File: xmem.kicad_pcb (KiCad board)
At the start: 2 copper layers, 6 parts, among them P1 CONN_02X18, U1 AS6C1008-55SIN, U2 SN74AHC573

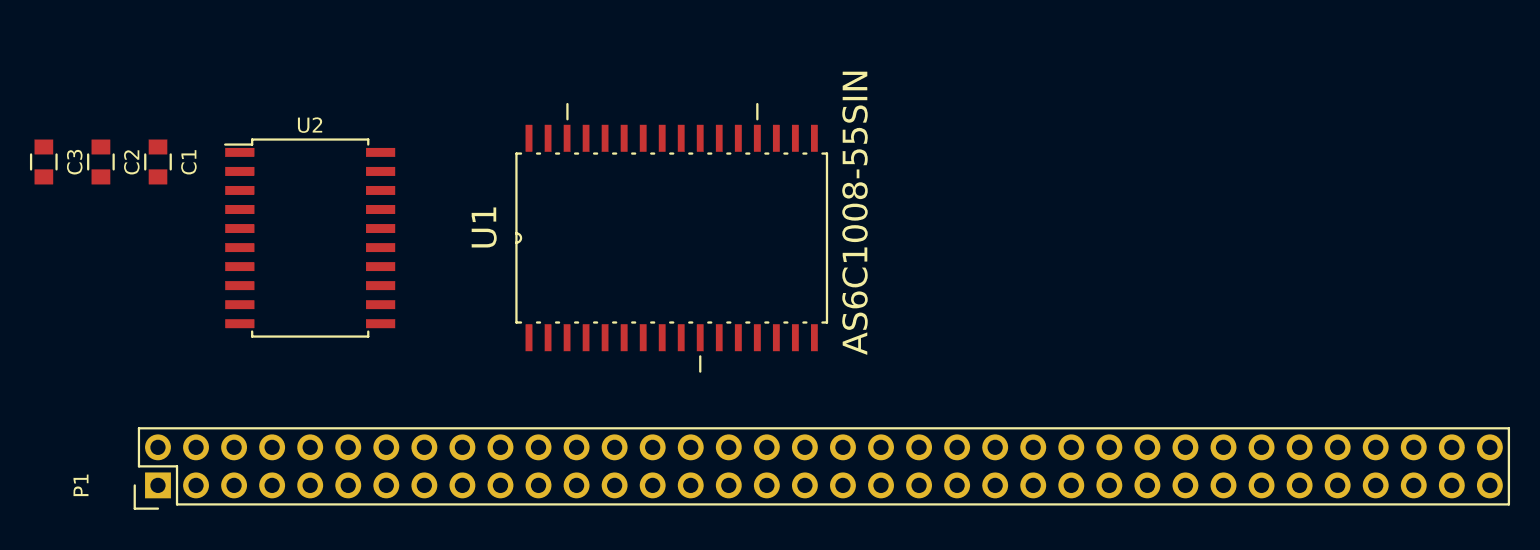
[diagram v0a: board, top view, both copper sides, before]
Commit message: Update to connect remaining pins and update footprints
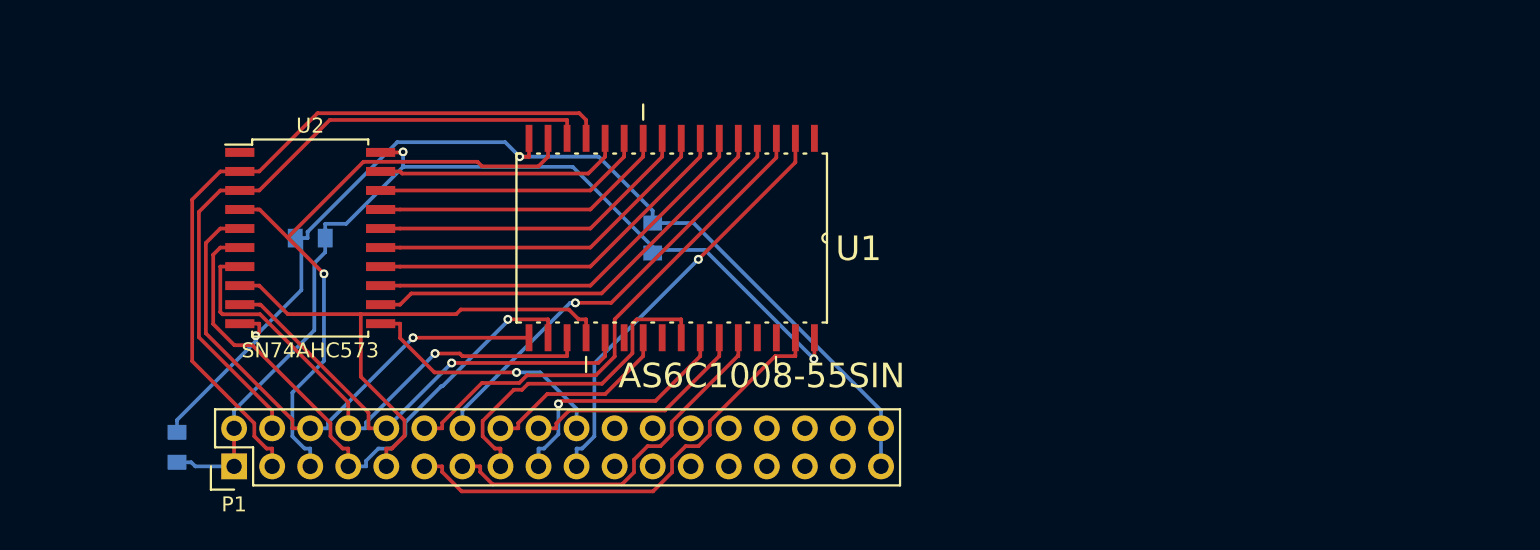
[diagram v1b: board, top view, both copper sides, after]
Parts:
- C1, C2, C3: moved to B.Cu
- P1: footprint Pin_Headers:Pin_Header_Straight_2x36 -> Pin_Headers:Pin_Header_Straight_2x18
- moved C2 37.2 mm to (139.7, 104.1), turned to 90 degrees
- moved C3 21.0 mm to (108.0, 118.1), turned to 90 degrees
- moved C1 11.4 mm to (116.8, 104.1), turned to 180 degrees
- moved P1 5.24 mm to (111.8, 119.4)
- turned U1 to 270 degrees
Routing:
- net GND: track 0.00 -> 74.1 mm, vias 0 -> 2
- net VCC: track 0.00 -> 66.4 mm, vias 0 -> 2
- net /D0: track 0.00 -> 50.3 mm
- net /D1: track 0.00 -> 44.8 mm
- net /D2: track 0.00 -> 42.9 mm, vias 0 -> 1
- net /D4: track 0.00 -> 40.2 mm, vias 0 -> 1
- net /D6: track 0.00 -> 37.6 mm
- net /D3: track 0.00 -> 35.9 mm, vias 0 -> 1
- net /D5: track 0.00 -> 35.3 mm, vias 0 -> 1
- net /A14: track 0.00 -> 33.9 mm
- net /A15: track 0.00 -> 31.7 mm
- net /D7: track 0.00 -> 31.6 mm, vias 0 -> 1
- net /A7: track 0.00 -> 29.2 mm
- net /A12: track 0.00 -> 29.1 mm, vias 0 -> 1
- net /A16: track 0.00 -> 28.2 mm, vias 0 -> 1
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
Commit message: Add flood fill ground plane. Fix close tracks. Add text
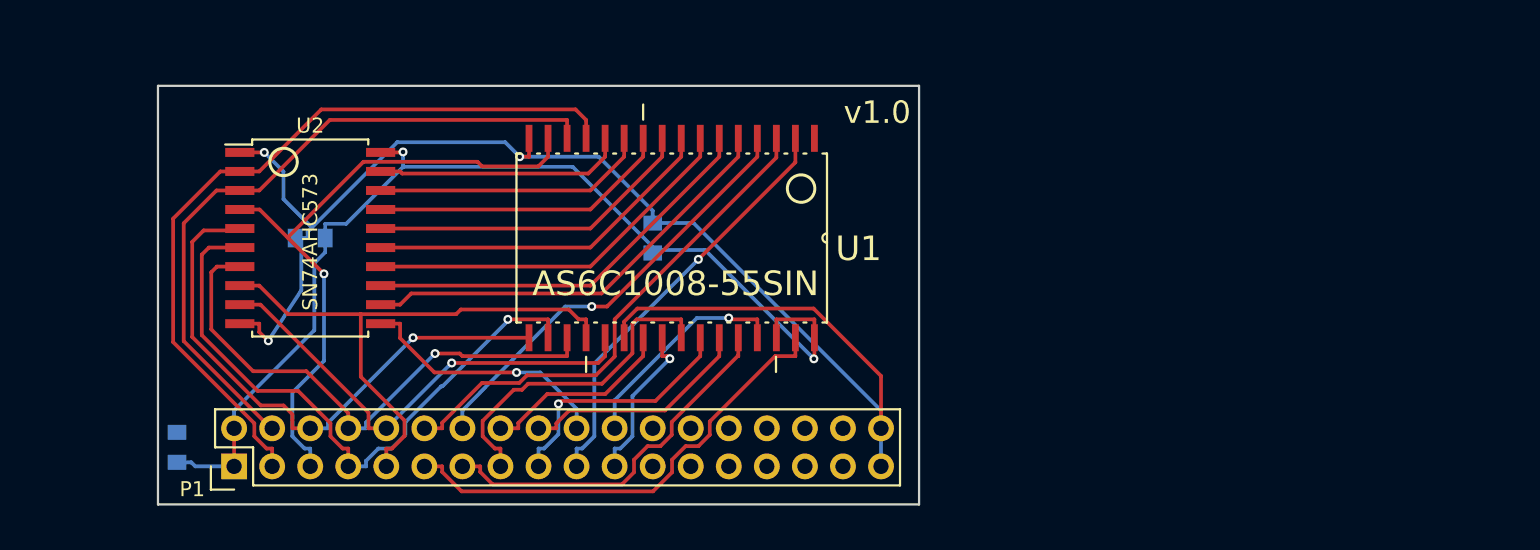
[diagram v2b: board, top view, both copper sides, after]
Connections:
- U1 pad 22: Net-(U1-Pad22) -> GND
- U1 pad 24: Net-(U1-Pad24) -> /~RD
- U1 pad 29: Net-(U1-Pad29) -> /~WR
- U1 pad 30: Net-(U1-Pad30) -> VCC
- U2 pad 1: Net-(U2-Pad1) -> GND
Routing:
- net GND: track 74.1 -> 97.6 mm, vias 2 -> 3
- net /~WR: track 0.00 -> 14.9 mm, vias 0 -> 1
- net /~RD: track 0.00 -> 10.7 mm, vias 0 -> 1
- net VCC: track 66.4 -> 71.4 mm
- net /D3: track 35.9 -> 38.2 mm
- net /D4: track 40.2 -> 42.1 mm
- net /D0: track 50.3 -> 51.6 mm
- net /D5: track 35.3 -> 36.5 mm
- net /D1: track 44.8 -> 46.0 mm
- added copper zone on B.Cu, net GND
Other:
- board outline added: 50.8 x 27.9 mm
- board text added: "June 2016"
- board text added: "SRAM expansion"
- board text added: "https://github.com/cduk/xmem"
- board text added: "v1.0"

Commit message: RC1 - WIP
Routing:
- added copper zone on F.Cu, net GND
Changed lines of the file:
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@@
   (segment (start 108.396 103.155) (end 108.396 111.017) (width 0.25) (layer F.Cu) (net 22))
   (segment (start 110.586 100.965) (end 108.396 103.155) (width 0.25) (layer F.Cu) (net 22))
-  (segment (start 112.14 100.965) (end 110.586 100.965) (width 0.25) (layer F.Cu) (net 22) (status 400000))
+  (segment (start 112.14 100.965) (end 110.586 100.965) (width 0.25) (layer F.Cu) (net 22))
   (via (at 117.759 106.532) (size 0.6) (layers F.Cu B.Cu) (net 23))
   (segment (start 132.715 98.7122) (end 132.715 97.4852) (width 0.25) (layer F.Cu) (net 23))
@@
     (connect_pads (clearance 0.508))
     (min_thickness 0.254)
+    (fill yes (arc_segments 16) (thermal_gap 0.508) (thermal_bridge_width 0.508))
+    (polygon
+      (pts
+        (xy 157.48 121.92) (xy 106.68 121.92) (xy 106.68 93.98) (xy 157.48 93.98) (xy 157.48 121.92)
+      )
+    )
+  )
+  (zone (net 2) (net_name GND) (layer F.Cu) (hatch edge 0.508)
+    (connect_pads (clearance 0.508))
+    (min_thickness 0.254)

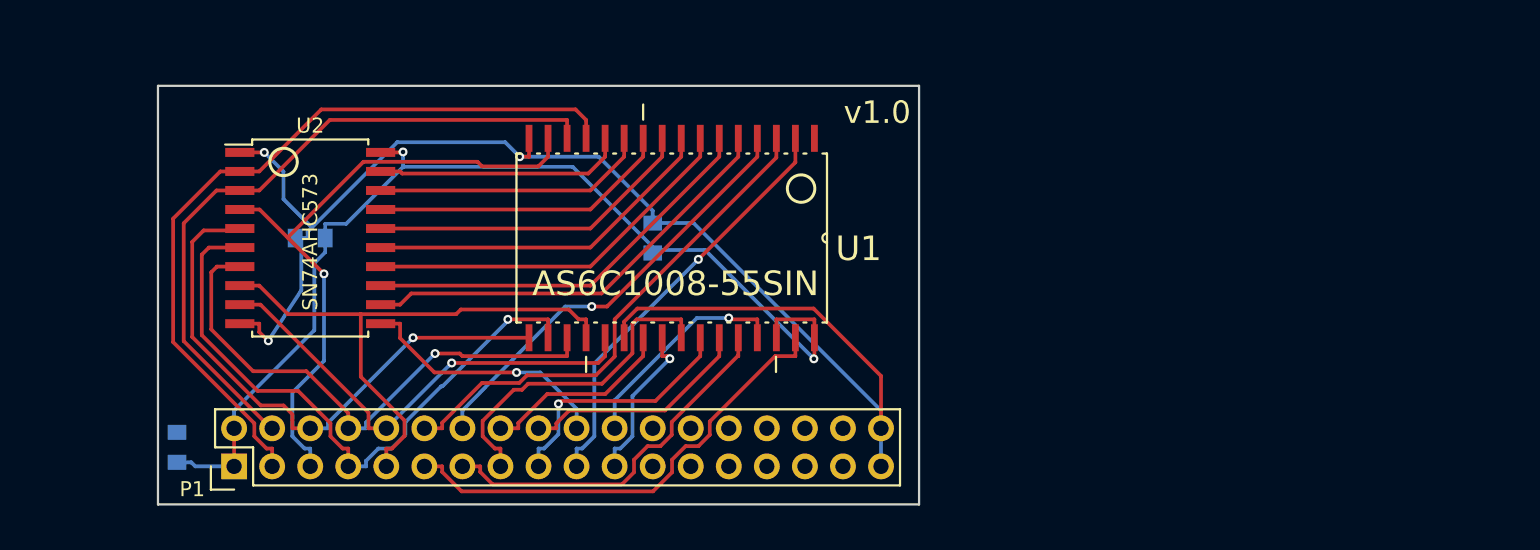
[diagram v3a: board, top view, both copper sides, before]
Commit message: Add stitching vias
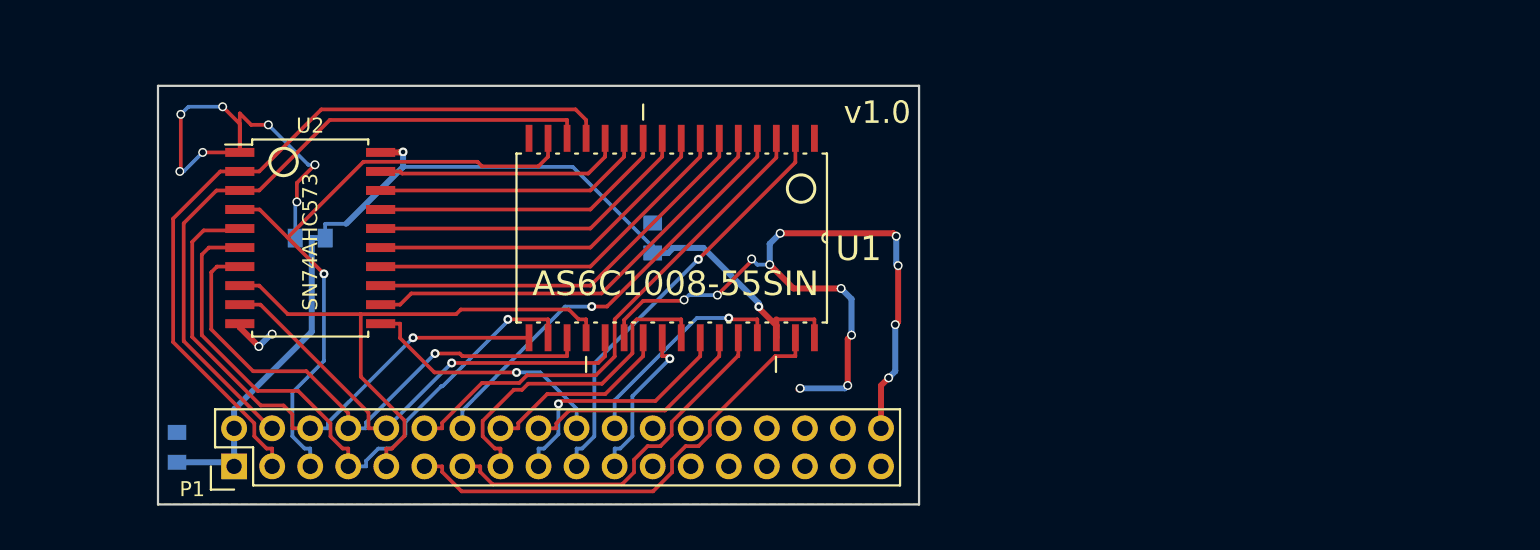
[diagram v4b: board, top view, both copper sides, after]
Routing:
- net GND: track 97.6 -> 85.1 mm, vias 3 -> 22
- net VCC: track 71.4 -> 67.3 mm
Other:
- net class GND added: clearance 0.2, trace_width 0.4, via_dia 0.6, via_drill 0.4
- net class VCC added: clearance 0.2, trace_width 0.4, via_dia 0.6, via_drill 0.4

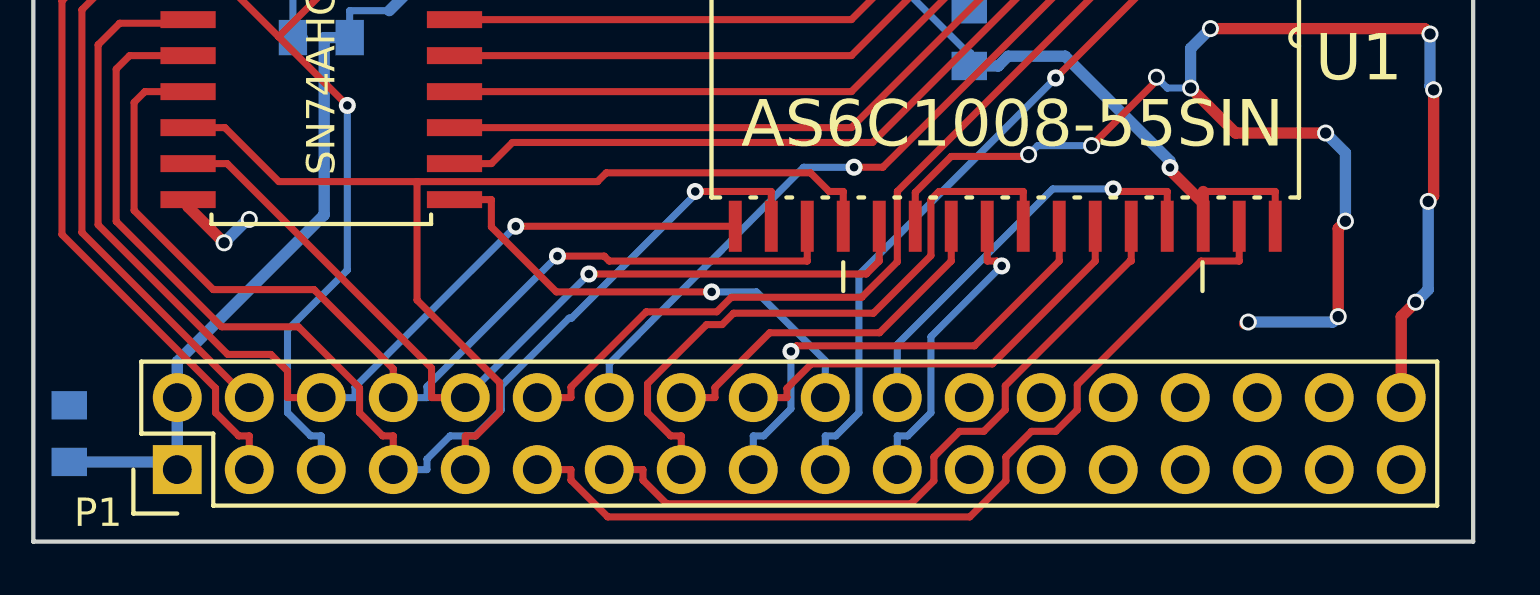
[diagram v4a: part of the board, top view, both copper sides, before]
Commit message: Add pin labels
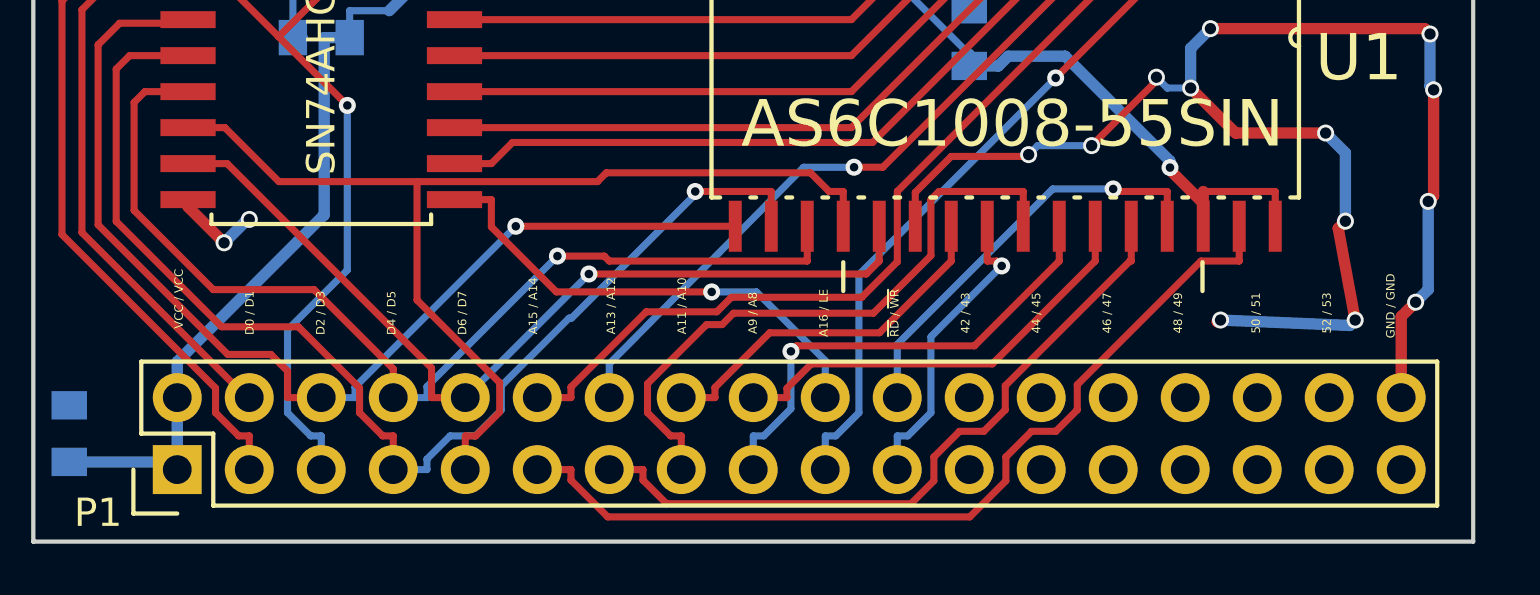
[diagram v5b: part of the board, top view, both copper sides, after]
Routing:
- net GND: track 85.1 -> 86.9 mm
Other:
- board text added: "42 / 43"
- board text added: "44 / 45"
- board text added: "46 / 47"
- board text added: "48 / 49"
- board text added: "50 / 51"
- board text added: "52 / 53"
- board text added: "A11 / A10"
- board text added: "A13 / A12"
- board text added: "A15 / A14"
- board text added: "A16 / LE"
- board text added: "A9 / A8"
- board text added: "D0 / D1"
- board text added: "D2 / D3"
- board text added: "D4 / D5"
- board text added: "D6 / D7"
- board text added: "GND / GND"
- board text added: "VCC / VCC"
- board text added: "~RD~ / ~WR"
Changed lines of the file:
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@@
     (area 106.604999 93.904999 157.555001 121.995001)
     (thickness 1.6)
-    (drawings 10)
+    (drawings 28)
     (tracks 374)
     (zones 0)
@@
     )
   )
+  (gr_text "GND / GND" (at 154.566 113.604 90) (layer F.SilkS)
+    (effects (font (size 0.3 0.3) (thickness 0.075)))
+  )
+  (gr_text "52 / 53" (at 152.316 113.854 90) (layer F.SilkS)
+    (effects (font (size 0.3 0.3) (thickness 0.075)))
+  )
+  (gr_text "50 / 51" (at 149.816 113.854 90) (layer F.SilkS)
+    (effects (font (size 0.3 0.3) (thickness 0.075)))
+  )
+  (gr_text "48 / 49" (at 147.066 113.854 90) (layer F.SilkS)
+    (effects (font (size 0.3 0.3) (thickness 0.075)))
+  )
+  (gr_text "46 / 47" (at 144.566 113.854 90) (layer F.SilkS)
+    (effects (font (size 0.3 0.3) (thickness 0.075)))
+  )
+  (gr_text "44 / 45" (at 142.066 113.854 90) (layer F.SilkS)
+    (effects (font (size 0.3 0.3) (thickness 0.075)))
+  )
+  (gr_text "42 / 43" (at 139.566 113.854 90) (layer F.SilkS)
+    (effects (font (size 0.3 0.3) (thickness 0.075)))
+  )
+  (gr_text "~RD~ / ~WR" (at 137.066 113.854 90) (layer F.SilkS)
+    (effects (font (size 0.3 0.3) (thickness 0.075)))
+  )
+  (gr_text "A16 / LE" (at 134.566 113.854 90) (layer F.SilkS)
+    (effects (font (size 0.3 0.3) (thickness 0.075)))
+  )
+  (gr_text "A9 / A8" (at 132.066 113.854 90) (layer F.SilkS)
+    (effects (font (size 0.3 0.3) (thickness 0.075)))
+  )
+  (gr_text "A11 / A10" (at 129.566 113.604 90) (layer F.SilkS)
+    (effects (font (size 0.3 0.3) (thickness 0.075)))
+  )
+  (gr_text "A13 / A12" (at 127.066 113.604 90) (layer F.SilkS)
+    (effects (font (size 0.3 0.3) (thickness 0.075)))
+  )
+  (gr_text "A15 / A14" (at 124.316 113.604 90) (layer F.SilkS)
+    (effects (font (size 0.3 0.3) (thickness 0.075)))
+  )
+  (gr_text "D6 / D7" (at 121.816 113.854 90) (layer F.SilkS)
+    (effects (font (size 0.3 0.3) (thickness 0.075)))
+  )
+  (gr_text "D4 / D5" (at 119.316 113.854 90) (layer F.SilkS)
+    (effects (font (size 0.3 0.3) (thickness 0.075)))
+  )
+  (gr_text "D2 / D3" (at 116.816 113.854 90) (layer F.SilkS)
+    (effects (font (size 0.3 0.3) (thickness 0.075)))
+  )
+  (gr_text "D0 / D1" (at 114.316 113.854 90) (layer F.SilkS)
+    (effects (font (size 0.3 0.3) (thickness 0.075)))
+  )
+  (gr_text "VCC / VCC" (at 111.816 113.354 90) (layer F.SilkS)
+    (effects (font (size 0.3 0.3) (thickness 0.075)))
+  )
   (gr_text "June 2016" (at 150.368 102.108) (layer B.SilkS)
     (effects (font (size 1.5 1.5) (thickness 0.3)) (justify mirror))
@@
   (via (at 114.3 110.5535) (size 0.6) (drill 0.4) (layers F.Cu B.Cu) (net 2))
   (segment (start 154.94 116.84) (end 154.94 113.9825) (width 0.4) (layer F.Cu) (net 2))
-  (segment (start 149.479 114.2365) (end 149.4155 114.2365) (width 0.4) (layer F.Cu) (net 2))
-  (segment (start 149.5425 114.173) (end 149.479 114.2365) (width 0.4) (layer F.Cu) (net 2))
-  (via (at 149.5425 114.173) (size 0.6) (drill 0.4) (layers F.Cu B.Cu) (net 2))
-  (segment (start 152.527 114.173) (end 149.5425 114.173) (width 0.4) (layer B.Cu) (net 2))
-  (segment (start 152.7175 113.9825) (end 152.527 114.173) (width 0.4) (layer B.Cu) (net 2))
-  (via (at 152.7175 113.9825) (size 0.6) (drill 0.4) (layers F.Cu B.Cu) (net 2))
-  (segment (start 152.7175 110.871) (end 152.7175 113.9825) (width 0.4) (layer F.Cu) (net 2))
+  (segment (start 148.5025 114.1675) (end 148.439 114.1675) (width 0.4) (layer F.Cu) (net 2))
+  (segment (start 148.566 114.104) (end 148.5025 114.1675) (width 0.4) (layer F.Cu) (net 2))
+  (via (at 148.566 114.104) (size 0.6) (drill 0.4) (layers F.Cu B.Cu) (net 2))
+  (segment (start 153.1255 114.2945) (end 148.566 114.104) (width 0.4) (layer B.Cu) (net 2))
+  (segment (start 153.316 114.104) (end 153.1255 114.2945) (width 0.4) (layer B.Cu) (net 2))
+  (via (at 153.316 114.104) (size 0.6) (drill 0.4) (layers F.Cu B.Cu) (net 2))
+  (segment (start 152.7175 110.871) (end 153.316 114.104) (width 0.4) (layer F.Cu) (net 2))
   (segment (start 152.9715 110.617) (end 152.7175 110.871) (width 0.4) (layer F.Cu) (net 2))
   (via (at 152.9715 110.617) (size 0.6) (drill 0.4) (layers F.Cu B.Cu) (net 2))
